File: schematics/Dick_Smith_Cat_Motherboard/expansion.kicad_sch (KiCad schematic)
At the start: 24 parts, among them J2 Expansion Connector, J5 Edge Connector

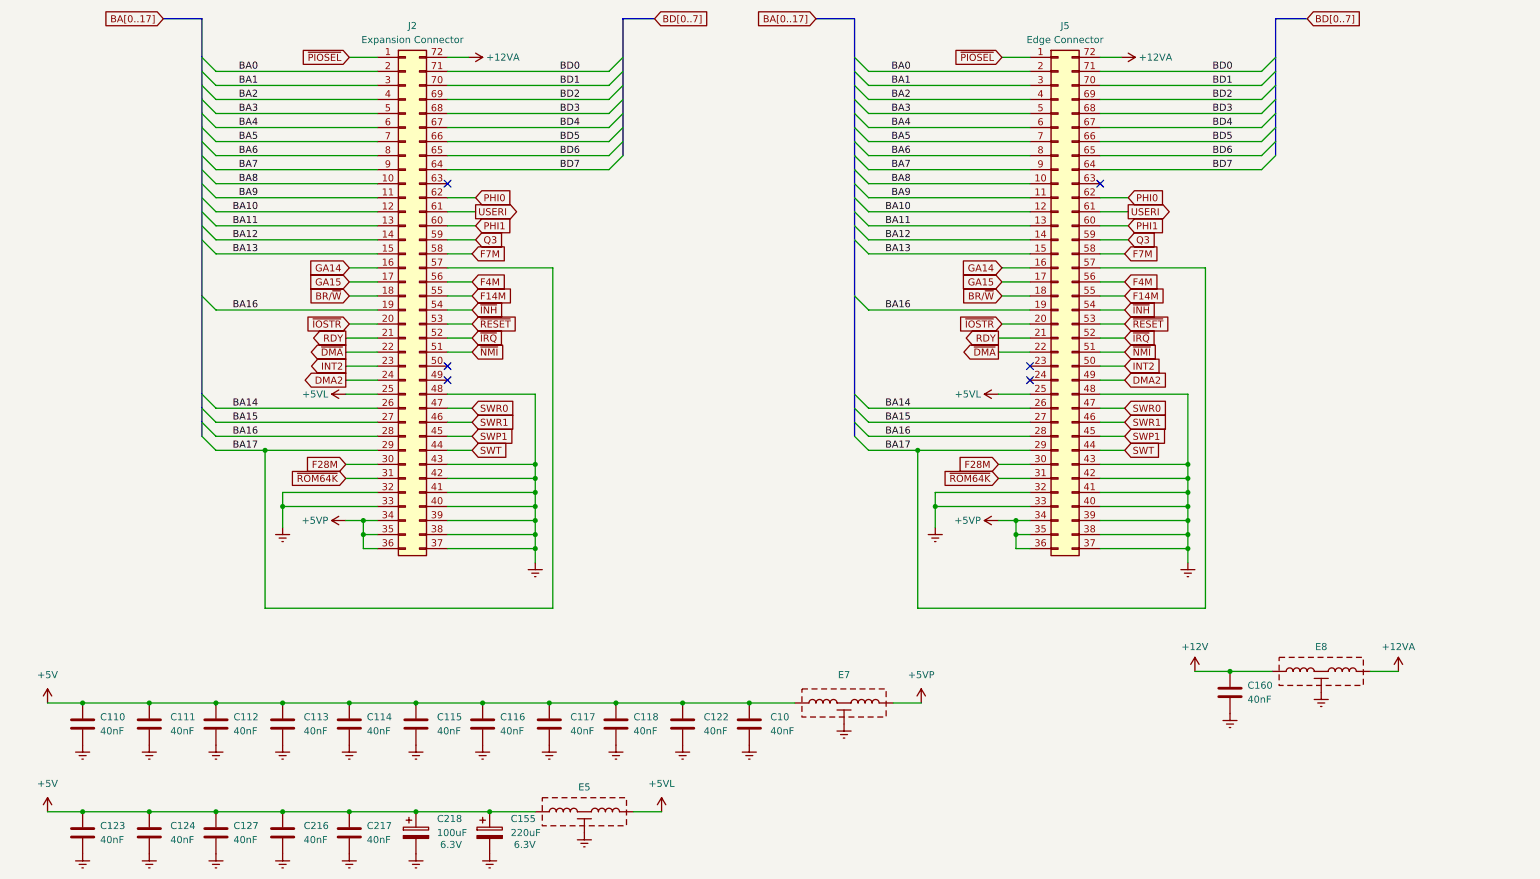
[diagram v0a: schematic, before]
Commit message: Add more connector pinouts to the schematics
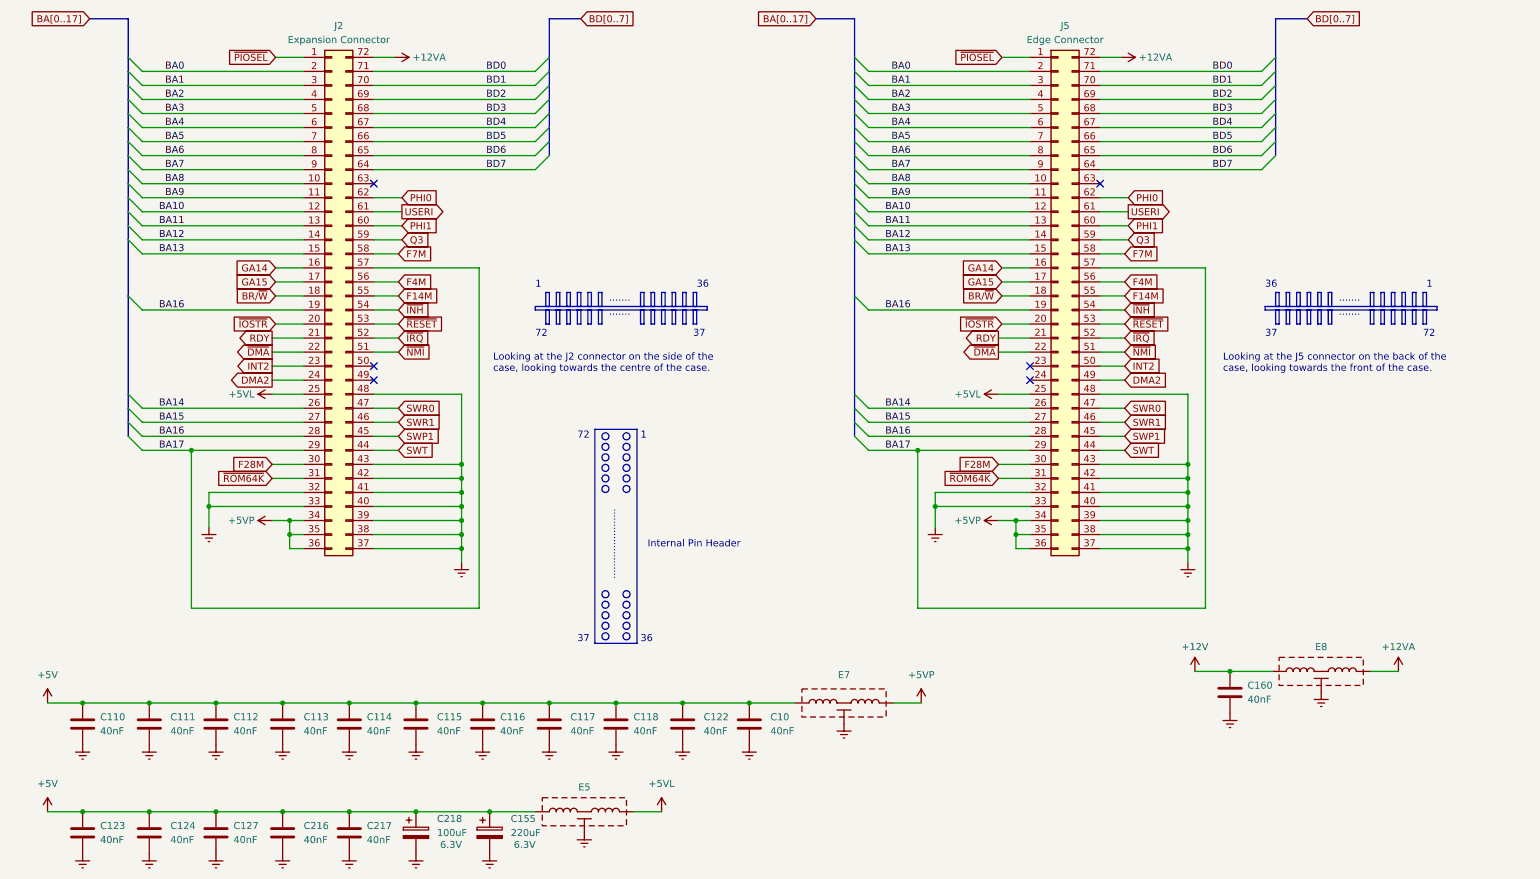
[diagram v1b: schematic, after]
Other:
- note added: "......."
- note added: "......................."
- note added: "1"
- note added: "36"
- note added: "37"
- note added: "72"
- note added: "Internal Pin Header"
- note added: "Looking at the J2 connector on the side of the case, looking towards the centre of the case."
- note added: "Looking at the J5 connector on the back of the case, looking towards the front of the case."
- moved on the sheet: J2
